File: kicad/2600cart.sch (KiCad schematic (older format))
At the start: 4 parts, among them U1 2600Cartridge, U2 74LS04, U3 2732

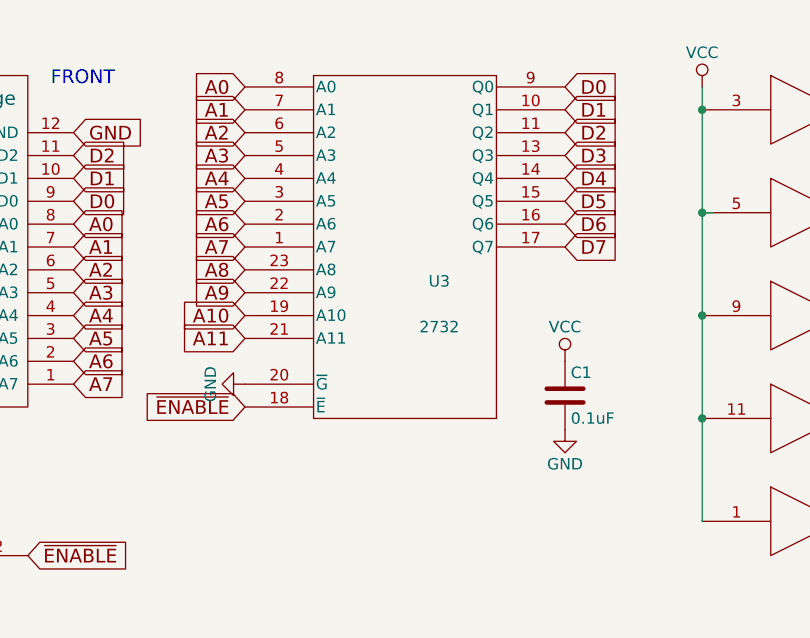
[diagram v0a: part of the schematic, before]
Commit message: fix schematic for new KiCad version, export netlist, import netlist, and run DRC
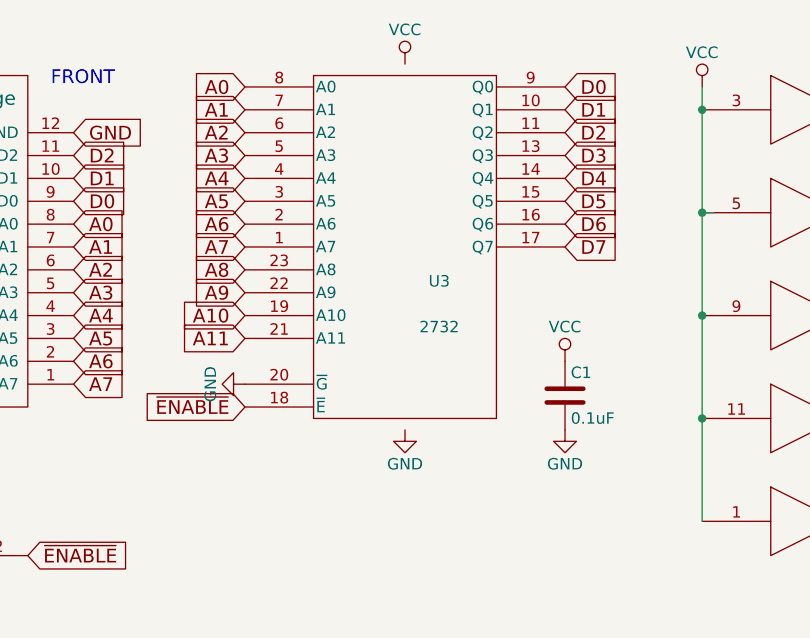
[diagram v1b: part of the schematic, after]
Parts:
- C1: footprint Capacitors_ThroughHole:C_Disc_D3_P2.5 -> Capacitor_THT:C_Disc_D3.0mm_W2.0mm_P2.50mm
- U2: footprint Housings_DIP:DIP-14_W7.62mm -> Package_DIP:DIP-14_W7.62mm
- U3: footprint Housings_DIP:DIP-24_W15.24mm -> Package_DIP:DIP-24_W15.24mm
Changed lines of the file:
@@
 F 0 "U2" H 6995 2065 50  0000 C CNN
 F 1 "74LS04" H 6990 1825 50  0000 C CNN
-F 2 "Housings_DIP:DIP-14_W7.62mm" H 6800 1950 50  0001 C CNN
+F 2 "Package_DIP:DIP-14_W7.62mm" H 6800 1950 50  0001 C CNN
 F 3 "" H 6800 1950 50  0000 C CNN
 	2    6800 1950
@@
 F 0 "U2" H 6995 2515 50  0000 C CNN
 F 1 "74LS04" H 6990 2275 50  0000 C CNN
-F 2 "Housings_DIP:DIP-14_W7.62mm" H 6800 2400 50  0001 C CNN
+F 2 "Package_DIP:DIP-14_W7.62mm" H 6800 2400 50  0001 C CNN
 F 3 "" H 6800 2400 50  0000 C CNN
 	3    6800 2400
@@
 F 0 "U2" H 6995 3865 50  0000 C CNN
 F 1 "74LS04" H 6990 3625 50  0000 C CNN
-F 2 "Housings_DIP:DIP-14_W7.62mm" H 6800 3750 50  0001 C CNN
+F 2 "Package_DIP:DIP-14_W7.62mm" H 6800 3750 50  0001 C CNN
 F 3 "" H 6800 3750 50  0000 C CNN
 	1    6800 3750
@@
 F 0 "U2" H 6995 2965 50  0000 C CNN
 F 1 "74LS04" H 6990 2725 50  0000 C CNN
-F 2 "Housings_DIP:DIP-14_W7.62mm" H 6800 2850 50  0001 C CNN
+F 2 "Package_DIP:DIP-14_W7.62mm" H 6800 2850 50  0001 C CNN
 F 3 "" H 6800 2850 50  0000 C CNN
 	4    6800 2850
@@
 F 0 "U2" H 6995 3415 50  0000 C CNN
 F 1 "74LS04" H 6990 3175 50  0000 C CNN
-F 2 "Housings_DIP:DIP-14_W7.62mm" H 6800 3300 50  0001 C CNN
+F 2 "Package_DIP:DIP-14_W7.62mm" H 6800 3300 50  0001 C CNN
 F 3 "" H 6800 3300 50  0000 C CNN
 	5    6800 3300
@@
 F 0 "U2" H 3145 4015 50  0000 C CNN
 F 1 "74LS04" H 3140 3775 50  0000 C CNN
-F 2 "Housings_DIP:DIP-14_W7.62mm" H 2950 3900 50  0001 C CNN
+F 2 "Package_DIP:DIP-14_W7.62mm" H 2950 3900 50  0001 C CNN
 F 3 "" H 2950 3900 50  0000 C CNN
 	6    2950 3900
@@
 F 0 "U3" H 5200 2400 50  0000 C CNN
 F 1 "2732" H 5200 2200 50  0000 C CNN
-F 2 "Housings_DIP:DIP-24_W15.24mm" H 5050 2550 50  0001 C CNN
+F 2 "Package_DIP:DIP-24_W15.24mm" H 5050 2550 50  0001 C CNN
 F 3 "" H 5050 2550 50  0000 C CNN
 	1    5050 2550
@@
 F 0 "C1" H 5775 3300 50  0000 L CNN
 F 1 "0.1uF" H 5775 3100 50  0000 L CNN
-F 2 "Capacitors_ThroughHole:C_Disc_D3_P2.5" H 5788 3050 50  0001 C CNN
+F 2 "Capacitor_THT:C_Disc_D3.0mm_W2.0mm_P2.50mm" H 5788 3050 50  0001 C CNN
 F 3 "" H 5750 3200 50  0000 C CNN
 	1    5750 3200
@@
 Wire Wire Line
 	6350 1950 6350 2400
+$Comp
+L 2600cart-rescue:VCC #PWR0101
+U 1 1 632BCB27
+P 5050 1750
+F 0 "#PWR0101" H 5050 1600 50  0001 C CNN
+F 1 "VCC" H 5050 1900 50  0000 C CNN
+F 2 "" H 5050 1750 50  0000 C CNN
+F 3 "" H 5050 1750 50  0000 C CNN
+	1    5050 1750
+	1    0    0    -1
+$EndComp
+$Comp
+L 2600cart-rescue:GND #PWR0102
+U 1 1 632C3779
+P 5050 3350
+F 0 "#PWR0102" H 5050 3100 50  0001 C CNN
+F 1 "GND" H 5050 3200 50  0000 C CNN
+F 2 "" H 5050 3350 50  0000 C CNN
+F 3 "" H 5050 3350 50  0000 C CNN
+	1    5050 3350
+	1    0    0    -1
+$EndComp
 $EndSCHEMATC
